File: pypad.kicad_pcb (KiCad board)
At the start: 2 copper layers, 100 x 100 mm, 64 parts, among them J1 Conn_01x05_Male, K1 SW_SPST, K10 SW_SPST, K11 SW_SPST, K12 SW_SPST, K13 SW_SPST, K14 SW_SPST, K15 SW_SPST, K16 SW_SPST, K17 SW_SPST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

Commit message: Routing attempt number 2
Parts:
- removed the REF** at (114.0, 71.5)
- removed the REF** at (84.2, 99.7)
- removed the REF** at (84.2, 42.5)
- removed the REF** at (46.1, 42.5)
- removed the REF** at (46.1, 99.7)
- added REF**: MountingHole_3.2mm_M3_Pad_Via, MountingHole:MountingHole_3.2mm_M3_Pad_Via, F.Cu at (120.4, 114.0)
- added REF**: MountingHole_3.2mm_M3_Pad_Via, MountingHole:MountingHole_3.2mm_M3_Pad_Via, F.Cu at (115.3, 24.9)
- added REF**: MountingHole_3.2mm_M3_Pad_Via, MountingHole:MountingHole_3.2mm_M3_Pad_Via, F.Cu at (28.4, 116.8)
- added REF**: MountingHole_3.2mm_M3_Pad_Via, MountingHole:MountingHole_3.2mm_M3_Pad_Via, F.Cu at (28.4, 24.9)
- D1, D10, D11, D12, D13, D14, D15, D16, D17, D18, D19, D2, D20, D3, D4, D5, D6, D7, D8, D9: footprint Diode_THT:D_DO-35_SOD27_P7.62mm_Horizontal -> PyPad_Footprints:D_DO-35_SOD27_P7.62mm_Horizontal; moved to F.Cu
- K1, K10, K11, K12, K13, K14, K15, K16, K17, K18, K19, K2, K20, K3, K4, K5, K6, K7, K8, K9: footprint Button_Switch_Keyboard:SW_Cherry_MX_1.00u_PCB -> PyPad_Footprints:SW_Cherry_MX_1.00u_PCB
- R1, R10, R4, R7: value R -> 82
- R11, R2, R5, R8: value R -> 56
- R12, R3, R6, R9: value R -> 33
- moved D1 11.1 mm to (42.9, 22.9), turned to 195 degrees
- moved D11 10.4 mm to (80.3, 22.9), turned to 195 degrees
- moved D14 10.0 mm to (79.9, 80.0), turned to 195 degrees
- moved D15 10.0 mm to (79.9, 99.1), turned to 195 degrees
- moved D4 10.0 mm to (41.8, 80.0), turned to 195 degrees
- moved D9 10.0 mm to (60.8, 80.0), turned to 195 degrees
- moved D10 10.0 mm to (60.8, 99.1), turned to 195 degrees
- moved D16 10.0 mm to (98.9, 22.9), turned to 195 degrees
- moved D20 10.0 mm to (98.9, 99.1), turned to 195 degrees
- moved D3 10.0 mm to (41.8, 61.0), turned to 195 degrees
- moved D5 10.0 mm to (41.8, 99.1), turned to 195 degrees
- moved D6 10.0 mm to (60.8, 22.9), turned to 195 degrees
- moved D12 10.0 mm to (79.9, 41.8), turned to 195 degrees
- moved D13 10.0 mm to (79.9, 61.0), turned to 195 degrees
- moved D17 10.0 mm to (98.9, 41.8), turned to 195 degrees
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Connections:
- R3 pad 2: Net-(R3-Pad2) -> /PA8
- R4 pad 2: /PB0 -> Net-(R4-Pad2)
- R6 pad 2: Net-(R6-Pad2) -> /PB6
- R9 pad 2: /PA8 -> Net-(R9-Pad2)
- U1 pad 12: Net-(R1-Pad2) -> Net-(R7-Pad2)
- U1 pad 13: Net-(R2-Pad2) -> Net-(R8-Pad2)
- U1 pad 14: Net-(R3-Pad2) -> Net-(R9-Pad2)
- U1 pad 24: Net-(R10-Pad2) -> Net-(R12-Pad2)
- U1 pad 26: Net-(R12-Pad2) -> Net-(R10-Pad2)
- U1 pad 27: Net-(R7-Pad2) -> /PB6
- U1 pad 6: Net-(R8-Pad2) -> Net-(R1-Pad2)
- U1 pad 7: /PB0 -> Net-(R2-Pad2)
- U1 pad 8: Net-(R5-Pad2) -> Net-(R4-Pad2)
- U1 pad 9: Net-(R6-Pad2) -> Net-(R5-Pad2)
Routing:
- net Net-(R4-Pad2): track 0.00 -> 84.8 mm, vias 0 -> 1
- net Net-(R6-Pad2): track 76.7 -> 0.00 mm, vias 1 -> 0
- net /PB0: track 75.0 -> 0.00 mm, vias 1 -> 0
- net /row4: track 172.4 -> 97.6 mm, vias 1 -> 2
- net Net-(R9-Pad2): track 0.00 -> 73.6 mm, vias 0 -> 1
- net Net-(R3-Pad2): track 55.6 -> 0.00 mm, vias 2 -> 0
- net /PB6: track 0.00 -> 53.7 mm, vias 0 -> 2
- net +3V3: track 54.8 -> 93.7 mm, vias 3 -> 8
- net Net-(R7-Pad2): track 57.5 -> 78.1 mm, vias 0 -> 1
- net Net-(R10-Pad2): track 59.5 -> 79.9 mm
- net /PA8: track 87.0 -> 68.6 mm, vias 1 -> 3
- net /TX1: track 102.7 -> 85.0 mm, vias 0 -> 2
- net Net-(R1-Pad2): track 50.5 -> 66.5 mm, vias 0 -> 1
- net Net-(R8-Pad2): track 90.3 -> 76.8 mm, vias 2 -> 1
- net /row1: track 81.7 -> 68.4 mm
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- removed copper zone on B.Cu, net GND

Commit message: Revision 2
Moved board around to allow M3 holes, rerouted using freeRouting and manually fixed.
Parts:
- removed REF** (x4): MountingHole_3.2mm_M3_Pad_Via, MountingHole:MountingHole_3.2mm_M3_Pad_Via
- added M1: MountingHole_3.2mm_M3_Pad_Via, MountingHole:MountingHole_3.2mm_M3_Pad_Via, F.Cu at (27.9, 24.6)
- added M2: MountingHole_3.2mm_M3_Pad_Via, MountingHole:MountingHole_3.2mm_M3_Pad_Via, F.Cu at (115.3, 24.6)
- added M3: MountingHole_3.2mm_M3_Pad_Via, MountingHole:MountingHole_3.2mm_M3_Pad_Via, F.Cu at (119.9, 112.8)
- added M4: MountingHole_3.2mm_M3_Pad_Via, MountingHole:MountingHole_3.2mm_M3_Pad_Via, F.Cu at (27.9, 117.6)
- moved U1 1.36 mm to (114.7, 49.4)
- moved D1 1.00 mm to (41.9, 22.9)
- moved D10 1.00 mm to (59.8, 99.1)
- moved D11 1.00 mm to (79.3, 22.9)
- moved D12 1.00 mm to (78.9, 41.8)
- moved D13 1.00 mm to (78.9, 61.0)
- moved D14 1.00 mm to (78.9, 80.0)
- moved D15 1.00 mm to (78.9, 99.1)
- moved D16 1.00 mm to (97.9, 22.9)
- moved D17 1.00 mm to (97.9, 41.8)
- moved D18 1.00 mm to (97.9, 61.0)
- moved D19 1.00 mm to (97.9, 80.0)
- moved D2 1.00 mm to (40.8, 41.8)
- moved D20 1.00 mm to (97.9, 99.1)
- moved D3 1.00 mm to (40.8, 61.0)
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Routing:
- net GND: track 0.00 -> 118.5 mm
- net +3V3: track 93.7 -> 142.6 mm, vias 8 -> 0
- net /row4: track 97.6 -> 135.1 mm
- net Net-(R10-Pad2): track 79.9 -> 61.0 mm, vias 1 -> 0
- net +5V: track 91.2 -> 108.1 mm, vias 4 -> 1
- net Net-(R4-Pad2): track 84.8 -> 69.4 mm, vias 1 -> 0
- net Net-(R7-Pad2): track 78.1 -> 65.1 mm
- net Net-(R11-Pad2): track 72.7 -> 60.4 mm, vias 1 -> 0
- net Net-(R5-Pad2): track 78.7 -> 69.2 mm, vias 3 -> 0
- net Net-(D4-Pad2): track 0.00 -> 8.75 mm
- net Net-(R8-Pad2): track 76.8 -> 68.3 mm
- net /TX1: track 85.0 -> 76.5 mm, vias 2 -> 0
- net Net-(R9-Pad2): track 73.6 -> 66.2 mm
- net Net-(R1-Pad2): track 66.5 -> 73.1 mm, vias 1 -> 0
- net Net-(R12-Pad2): track 65.9 -> 60.1 mm, vias 1 -> 0
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- added copper zone on B.Cu, net GND
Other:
- board text added: "*bonus io*"
- board text added: "3v3"
- board text added: "5v"
- board text added: "A15"
- board text added: "Blue"
- board text added: "C15"
- board text added: "Column 0: PB12"
- board text added: "Column 1: PB13"
- board text added: "Column 2: PB14"
- board text added: "Column 3: PB15"
- board text added: "Encoder: PA4 & PA5"
- board text added: "Gnd"
- board text added: "Green"
- board text added: "LED1"
- board text added: "LED2"
- board text added: "LED3"
- board text added: "LED4"
- board text added: "PA1"
- board text added: "PA2"
- board text added: "PA3"
- board text added: "PA6"
- board text added: "PA7"
- board text added: "PA8"
- board text added: "PB0"
- board text added: "PB1"
- board text added: "PB6"
- board text added: "PB7"
- board text added: "PB8"
- board text added: "PB9"
- board text added: "Red"
- board text added: "Row 0: PB2"
- board text added: "Row 1: PB3"
- board text added: "Row 2: PB4"
- board text added: "Row 4: PB5"
- board text added: "Row 5: PB10"
- board text added: "Switch: PC14"
- board text removed: "J1 pinout"
- board text removed: "TODO add matrix -> port mappings"

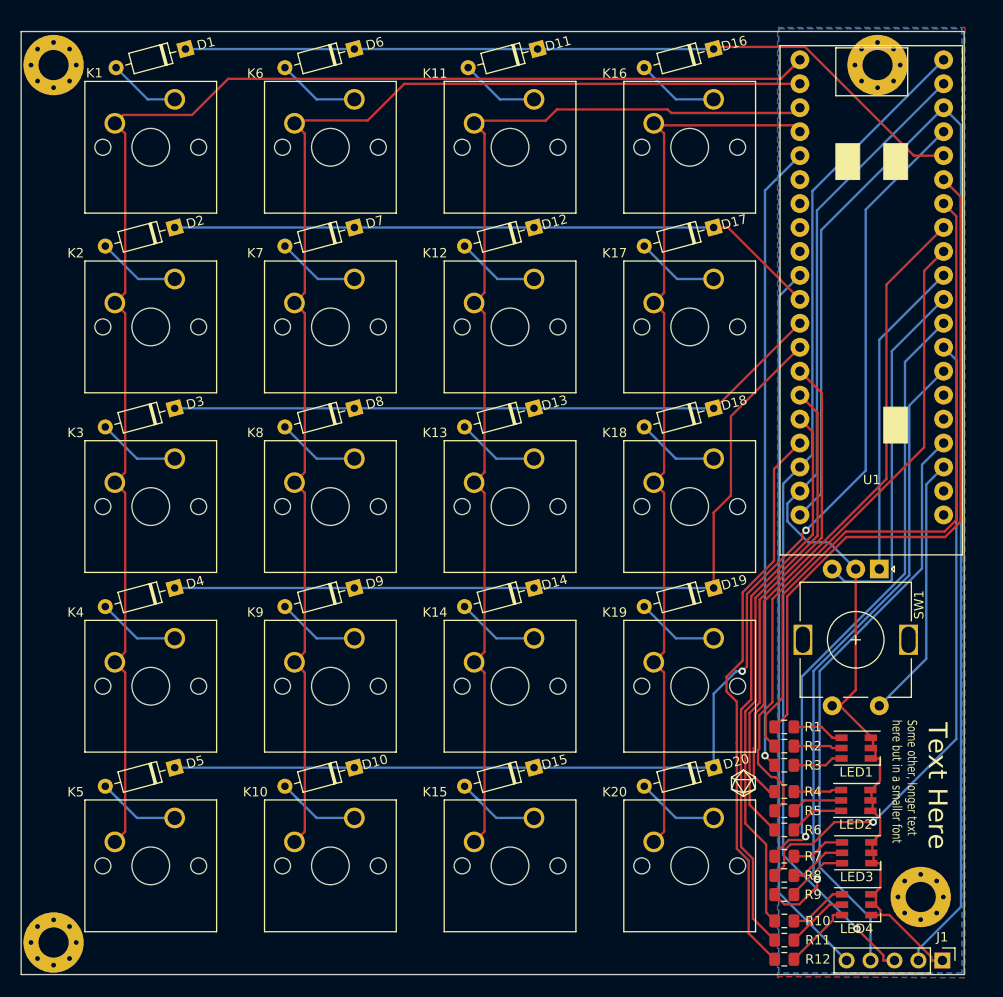
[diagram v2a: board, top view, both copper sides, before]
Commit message: Added underglow RGB, misc tweaks
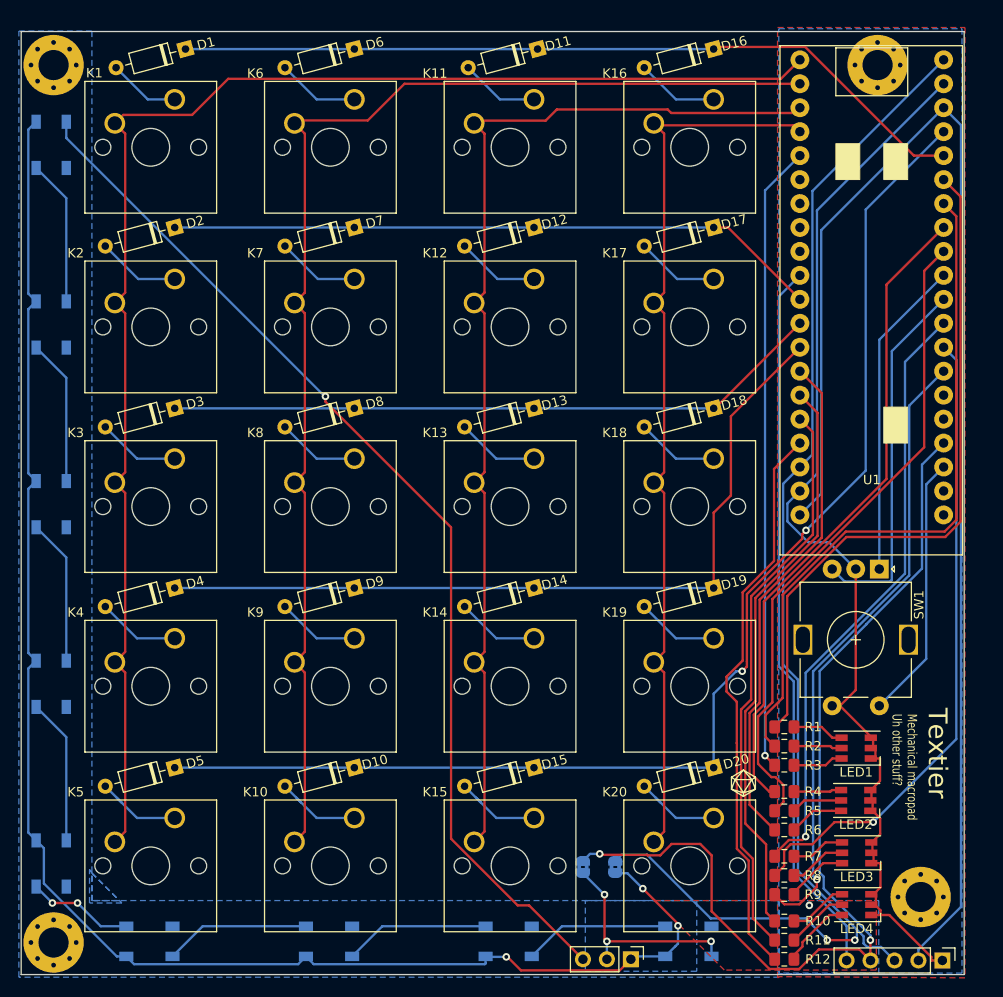
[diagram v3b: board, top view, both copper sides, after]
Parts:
- added J2: Conn_01x03_Male, Connector_PinHeader_2.54mm:PinHeader_1x03_P2.54mm_Vertical, F.Cu at (89.2, 119.4)
- added JP1: SolderJumper_2_Bridged, PyPad_Footprints:SolderJumper-2_P1.3mm_Bridged2BarCuttable_RoundedPad1.0x1.5mm, B.Cu at (87.5, 109.6)
- added JP2: SolderJumper_2_Bridged, PyPad_Footprints:SolderJumper-2_P1.3mm_Bridged2BarCuttable_RoundedPad1.0x1.5mm, B.Cu at (84.1, 109.6)
- added REF**: OSHW-Logo2_14.6x12mm_SilkScreen, Symbol:OSHW-Logo2_14.6x12mm_SilkScreen, B.Cu at (115.3, 35.4)
- added U10: SK6812, LED_SMD:LED_SK6812_PLCC4_5.0x5.0mm_P3.2mm, B.Cu at (27.7, 33.0)
- added U2: SK6812, LED_SMD:LED_SK6812_PLCC4_5.0x5.0mm_P3.2mm, B.Cu at (95.2, 117.5)
- added U3: SK6812, LED_SMD:LED_SK6812_PLCC4_5.0x5.0mm_P3.2mm, B.Cu at (76.2, 117.5)
- added U4: SK6812, LED_SMD:LED_SK6812_PLCC4_5.0x5.0mm_P3.2mm, B.Cu at (57.1, 117.5)
- added U5: SK6812, LED_SMD:LED_SK6812_PLCC4_5.0x5.0mm_P3.2mm, B.Cu at (38.1, 117.5)
- added U6: SK6812, LED_SMD:LED_SK6812_PLCC4_5.0x5.0mm_P3.2mm, B.Cu at (27.7, 109.2)
- added U7: SK6812, LED_SMD:LED_SK6812_PLCC4_5.0x5.0mm_P3.2mm, B.Cu at (27.7, 90.2)
- added U8: SK6812, LED_SMD:LED_SK6812_PLCC4_5.0x5.0mm_P3.2mm, B.Cu at (27.7, 71.1)
- added U9: SK6812, LED_SMD:LED_SK6812_PLCC4_5.0x5.0mm_P3.2mm, B.Cu at (27.7, 52.1)
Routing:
- net /Glow_5V: track 0.00 -> 168.9 mm, vias 0 -> 3
- net /Glow_Dout: track 0.00 -> 112.3 mm, vias 0 -> 1
- net /PC15: track 62.5 -> 104.2 mm, vias 0 -> 2
- net +5V: track 108.1 -> 139.6 mm, vias 1 -> 2
- net /Glow_Din: track 0.00 -> 22.9 mm, vias 0 -> 3
- net Net-(U7-Pad4): track 0.00 -> 15.5 mm
- net Net-(U4-Pad4): track 0.00 -> 15.5 mm
- net Net-(U8-Pad4): track 0.00 -> 15.5 mm
- net Net-(U3-Pad4): track 0.00 -> 15.5 mm
- net Net-(U10-Pad2): track 0.00 -> 15.5 mm
- net Net-(U6-Pad4): track 0.00 -> 15.5 mm
- net Net-(U2-Pad4): track 0.00 -> 15.5 mm
- net Net-(U5-Pad4): track 0.00 -> 11.3 mm, vias 0 -> 2
- net GND: vias 0 -> 1
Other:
- board text added: "5v->Vin"
- board text added: "Col 0: PB12"
- board text added: "Col 1: PB13"
- board text added: "Col 2: PB14"
- board text added: "Col 3: PB15"
- board text added: "Din"
- board text added: "Dout"
- board text added: "Glow"
- board text added: "LukeMoll/Textier"
- board text added: "Mechanical macropad Uh other stuff?"
- board text added: "PC15->Din"
- board text added: "Textier"
- board text added: "Vin"
- board text added: "github.com/"
- board text removed: "Column 0: PB12"
- board text removed: "Column 1: PB13"
- board text removed: "Column 2: PB14"
- board text removed: "Column 3: PB15"
- board text removed: "Some other, longer text here but in a smaller font"
- board text removed: "Text Here"

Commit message: Revision 3
Added rotary encoder footprint, reorganised and rerouted board to accommodate.
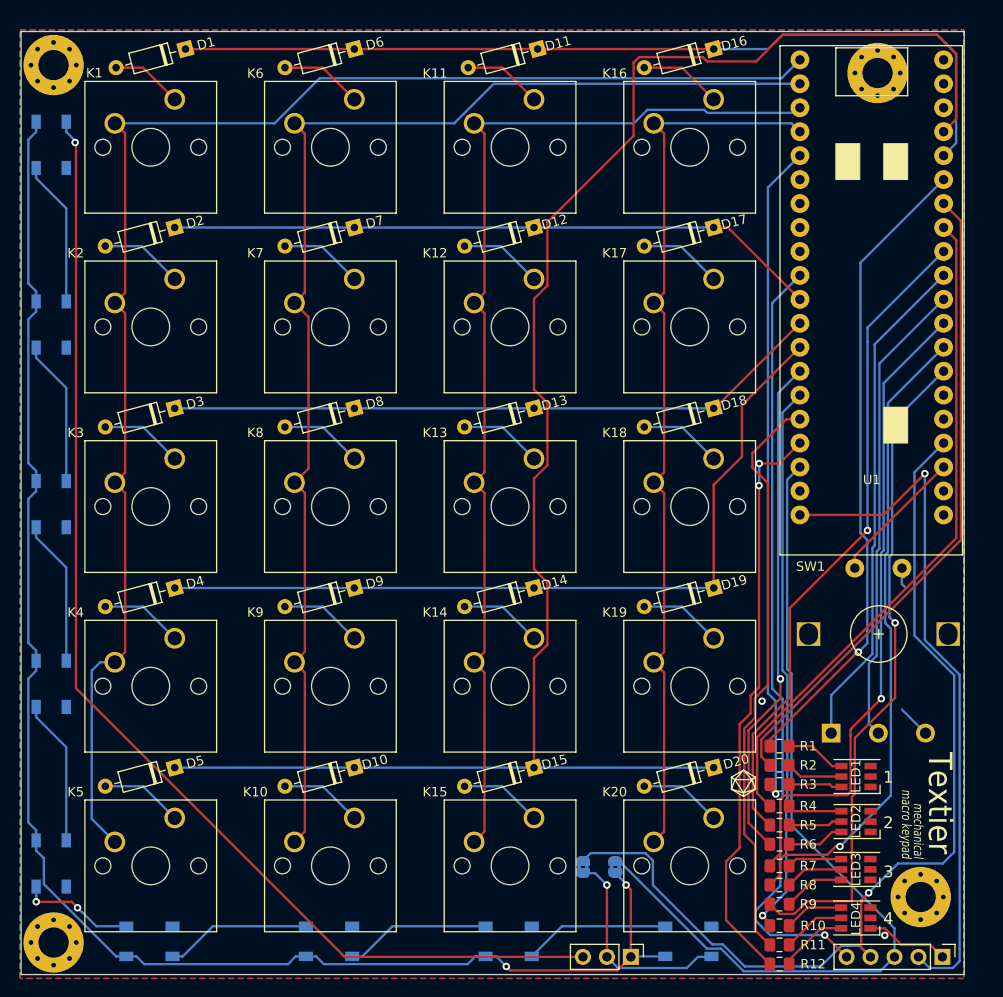
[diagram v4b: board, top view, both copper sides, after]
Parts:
- SW1: footprint Rotary_Encoder:RotaryEncoder_Alps_EC11E-Switch_Vertical_H20mm -> PyPad_Footprints:RotaryEncoder_Bourns_PEC16-4-Switch_Vertical_H20mm
- moved SW1 6.90 mm to (115.4, 84.9), turned to 90 degrees
- moved LED1 3.01 mm to (113.0, 100.0)
- moved LED2 2.24 mm to (113.0, 104.8)
- moved R1 2.09 mm to (104.9, 96.8)
- moved R2 2.09 mm to (104.9, 98.8)
- moved R3 2.09 mm to (104.9, 100.8)
- moved LED3 1.77 mm to (113.0, 109.9)
- moved R4 1.61 mm to (104.9, 103.1)
- moved R5 1.61 mm to (104.9, 105.2)
- moved R6 1.61 mm to (104.9, 107.2)
- moved LED4 1.42 mm to (113.0, 115.0)
- moved R7 1.14 mm to (104.9, 109.5)
- moved R8 1.14 mm to (104.9, 111.5)
- moved R9 1.14 mm to (104.9, 113.5)
- moved M2 0.84 mm to (115.3, 25.4)
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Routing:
- net GND: track 118.5 -> 15.9 mm, vias 1 -> 2
- net +3V3: track 142.6 -> 73.7 mm, vias 0 -> 1
- net /row4: track 135.1 -> 184.1 mm, vias 2 -> 0
- net +5V: track 139.6 -> 92.6 mm, vias 2 -> 0
- net Net-(SW1-PadA): track 34.0 -> 53.5 mm
- net /Glow_Dout: track 112.3 -> 126.0 mm
- net /PC14: track 28.1 -> 14.6 mm
- net /row0: track 85.3 -> 96.4 mm
- net Net-(SW1-PadB): track 39.0 -> 49.7 mm
- net /TX1: track 76.5 -> 82.7 mm, vias 0 -> 1
- net Net-(R1-Pad2): track 73.1 -> 68.4 mm, vias 0 -> 1
- net Net-(R7-Pad2): track 64.8 -> 69.1 mm
- net Net-(R9-Pad2): track 66.2 -> 70.4 mm
- net /PA8: track 66.6 -> 70.7 mm
- net /Glow_5V: track 168.9 -> 165.1 mm, vias 3 -> 2
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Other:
- board text added: "1"
- board text added: "2"
- board text added: "3"
- board text added: "4"
- board text added: "macro keypad"
- board text added: "mechanical"
- board text removed: "Mechanical macropad Uh other stuff?"
